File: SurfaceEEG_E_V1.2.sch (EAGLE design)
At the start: 9 parts, among them IC1 LMP7702

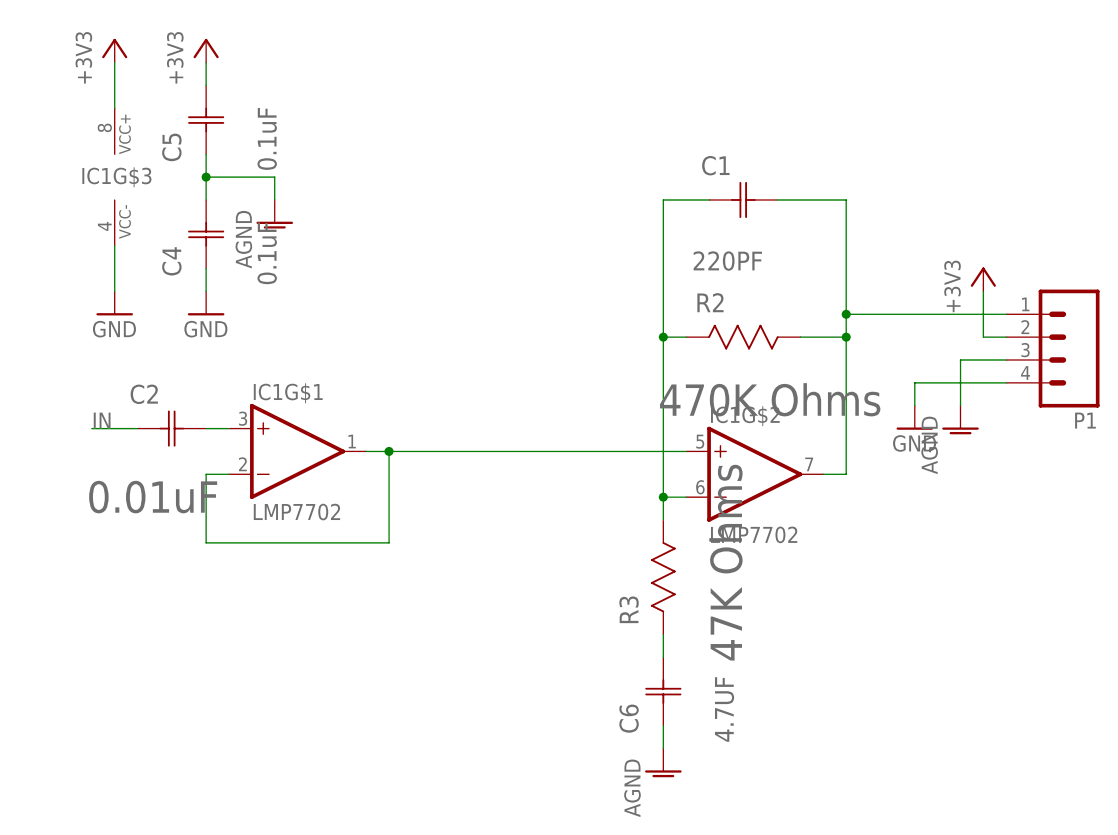
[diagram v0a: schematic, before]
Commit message: Add high pass filter to active electrode
Add high pass filter and trace PCB V1.2
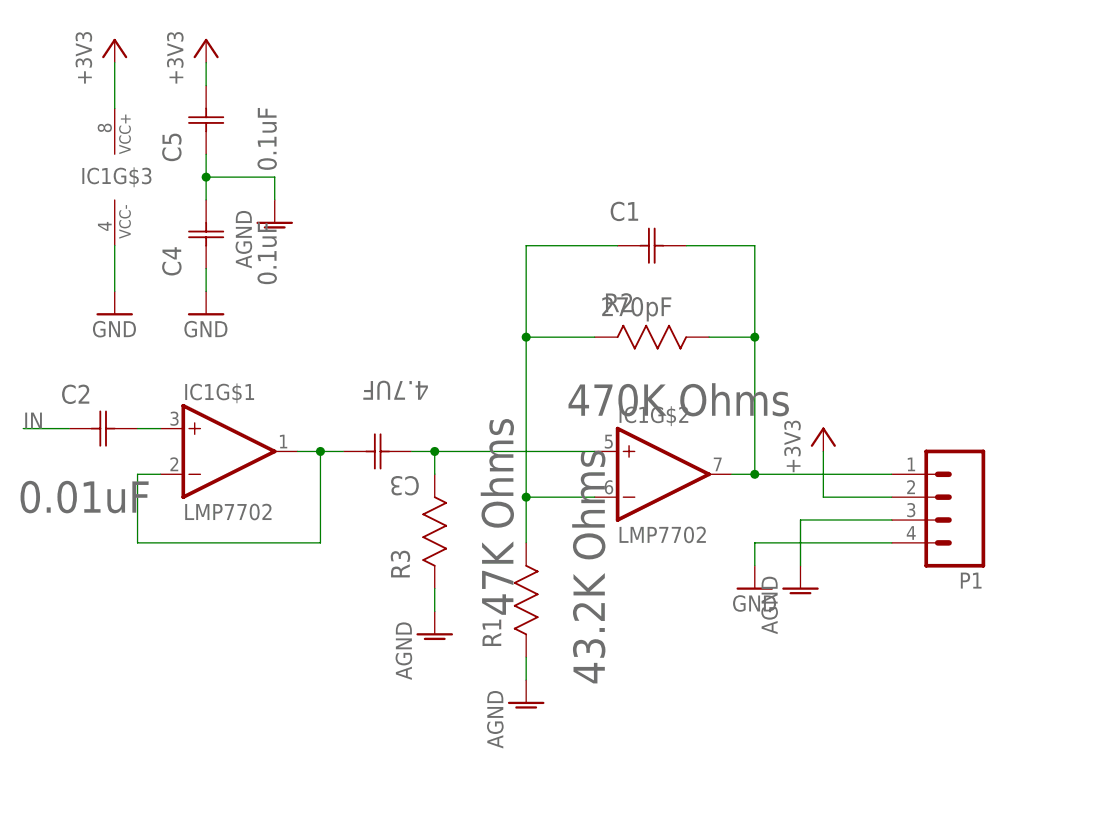
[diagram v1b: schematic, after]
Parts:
- removed C6: 4.7UF, (manufact)-capacitors-AVX-element14:06036D475MAT2A
- added C3: 4.7UF, (manufact)-capacitors-AVX-element14:06036D475MAT2A
- added R1: 43.2K Ohms, (manufact)-resistors-YAGEO-element14:RC0603FR-0743K2L
- C1: value 220PF -> 270pF; device (manufact)-capacitors-AVX-element14:0603ZC221KAT2A -> (manufact)-capacitors-AVX-element14:06035A271JAT2A
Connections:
- removed net N$4 (its old number): C1.C1, IC1G$2.IN-, R2.R2, R3.R1
- removed net N$6: C6.C2, R3.R2
- new net N$2: C1.C1, IC1G$2.IN-, R1.R1, R2.R2
- new net N$3: C3.C1, IC1G$2.IN+, R3.R1
- net AGND: now also R1.R2, R3.R2; no longer C6.C1
- net SHIELD: now also C3.C2; no longer IC1G$2.IN+
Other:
- moved on the sheet: C1, C2, IC1G$1, IC1G$2, P1, R2, R3
